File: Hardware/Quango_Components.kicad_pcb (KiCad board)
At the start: 4 copper layers, 80.8 x 100 mm, 186 parts, among them J1 Conn_01x12_Male, J2 Conn_01x16_Male, J3 Conn_01x12_Male, J4 Conn_01x12_Male, J5 SWD_Header, J6 Eurorack_10_pin_power, J7 Audio_Breakout, J8 Gate_Breakout, Q1 MMBT3904, U1 LM1117-3.3, U10 TL074, U11 TL074, U12 TL074, U13 TL074, U14 TL074, U15 TL074, U2 STM32G473V, U3 LM1117-5.0, U4 PS508, U5 MCP6002, U6 AS3364, U7 AS3364, U8 AD5676, U9 MCP48CMB21, Y1 8MHz 20pF

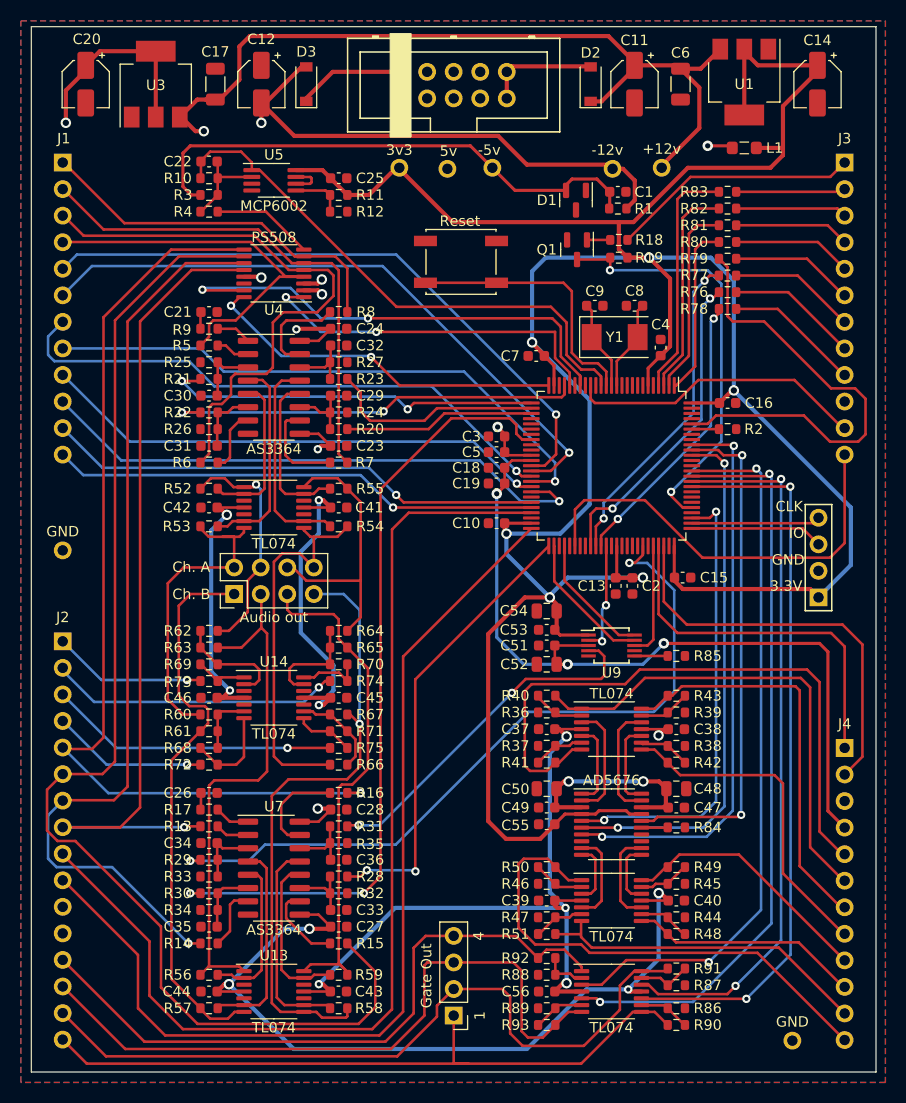
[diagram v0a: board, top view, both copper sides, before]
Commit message: Fixed OpAmp Power supply; component board annotations
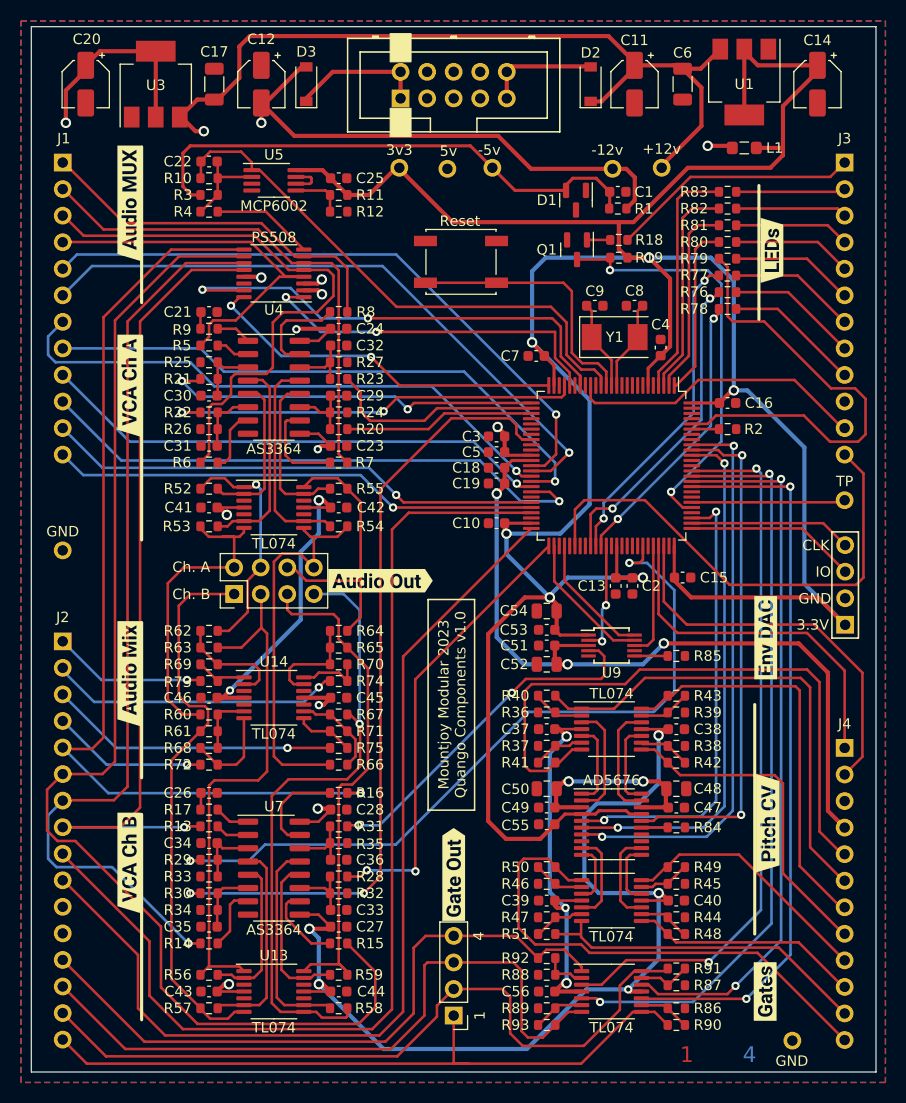
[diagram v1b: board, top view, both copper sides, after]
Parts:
- added FID1: Fiducial, Custom_Footprints:4_Layer_Markers, F.Cu at (115.8, 137.3)
- added J9: Test_Pin, Custom_Footprints:1mm_Test_Point, F.Cu at (127.9, 84.3)
- added kibuzzard-646A04C0: G***, kibuzzard-646A04C0, F.Cu at (59.5, 55.9)
- added kibuzzard-646A04E1: G***, kibuzzard-646A04E1, F.Cu at (59.5, 73.3)
- added kibuzzard-646A0551: G***, kibuzzard-646A0551, F.Cu at (59.5, 119.0)
- added kibuzzard-646A0570: G***, kibuzzard-646A0570, F.Cu at (59.5, 100.9)
- added kibuzzard-646A0602: G***, kibuzzard-646A0602, F.Cu at (83.5, 92.0)
- added kibuzzard-646A061F: G***, kibuzzard-646A061F, F.Cu at (90.5, 120.1)
- added kibuzzard-646A06F2: G***, kibuzzard-646A06F2, F.Cu at (120.5, 115.2)
- added kibuzzard-646A071F: G***, kibuzzard-646A071F, F.Cu at (120.3, 97.5)
- added kibuzzard-646A072B: G***, kibuzzard-646A072B, F.Cu at (120.3, 131.3)
- added kibuzzard-646A076E: G***, kibuzzard-646A076E, F.Cu at (121.0, 60.4)
- moved C41 12.4 mm to (67.1, 85.0), turned to 180 degrees
- moved C42 12.4 mm to (79.5, 85.0), turned to 0 degrees
- moved C44 12.4 mm to (79.5, 131.3), turned to 0 degrees
- moved C43 12.4 mm to (67.1, 131.3), turned to 180 degrees
- moved J5 3.66 mm to (128.0, 96.2)
- moved C6 0.20 mm to (112.4, 44.5)
- moved C17 0.10 mm to (67.6, 44.5)
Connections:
- U12 pad 11: +12V -> -12V
- U12 pad 4: -12V -> +12V
- U13 pad 11: +12V -> -12V
- U13 pad 4: -12V -> +12V
- U2 pad 81: unconnected-(U2-Pad81) -> Net-(U2-Pad81)
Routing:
- net Net-(U2-Pad81): track 0.00 -> 14.7 mm
- net /ChannelB_Level: track 41.0 -> 47.6 mm
- net +12V: track 258.8 -> 264.6 mm
- net -12V: track 257.8 -> 263.4 mm
- net +3.3V: track 310.6 -> 316.0 mm
- net /SWIO: track 12.8 -> 16.4 mm
- net /SWCLK: track 12.3 -> 15.5 mm
- net /USB_DP: track 39.2 -> 37.6 mm
- net /USB_DM: track 35.3 -> 34.0 mm
- net +3.3VA: track 227.7 -> 228.7 mm
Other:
- board text added: "Mountjoy Modular 2023 Quango Components v1.0"
- board text removed: "Audio out"
- board text removed: "Gate Out"

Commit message: Clean Up of Panel and Control boards
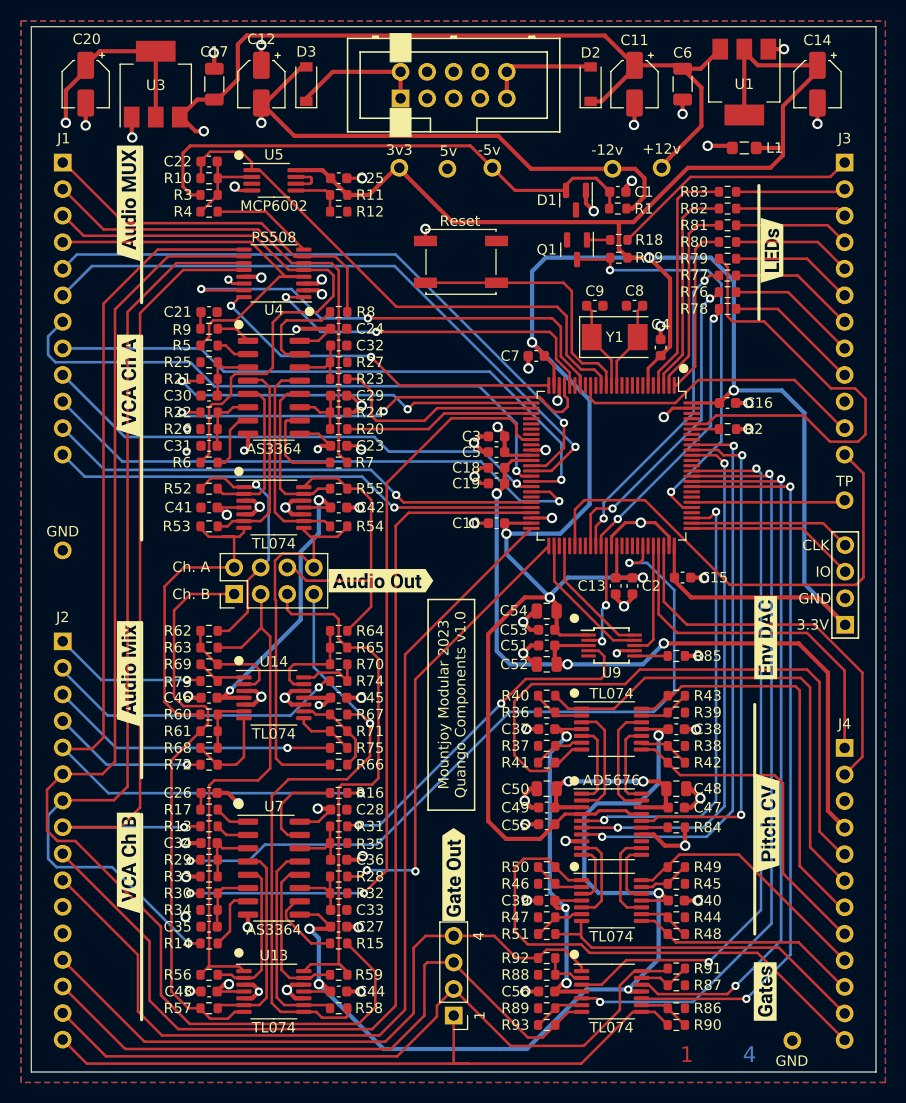
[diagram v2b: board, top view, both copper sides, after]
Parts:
- moved kibuzzard-646A04C0 0.05 mm to (59.4, 55.9)
- moved kibuzzard-646A04E1 0.05 mm to (59.4, 73.3)
- moved kibuzzard-646A0551 0.05 mm to (59.4, 119.0)
- moved kibuzzard-646A0570 0.05 mm to (59.4, 100.9)
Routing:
- net GND: track 0.00 -> 137.2 mm, vias 0 -> 65
- net /Gate3_Out: track 65.7 -> 62.4 mm
- net /OpAmps/AudioB3_Out: track 48.5 -> 51.5 mm
- net -12V: track 263.4 -> 266.3 mm
- net /Env1_Sustain: track 54.8 -> 57.4 mm
- net /EnvA2_DAC: track 39.9 -> 42.5 mm
- net /OpAmps/AudioA3_Out: track 27.2 -> 29.7 mm
- net /Env1_Release: track 55.7 -> 57.9 mm
- net /Gate2_Out: track 71.6 -> 69.5 mm
- net +3.3V: track 316.0 -> 317.9 mm
- net /OpAmps/AudioB1_Out: track 53.8 -> 55.2 mm
- net /Env1_Decay: track 61.4 -> 62.6 mm
- net /Audio3_Out: track 27.9 -> 29.0 mm
- net /AudioB3_In: track 118.9 -> 120.0 mm
- net /CV_OUT_A2: track 60.7 -> 61.6 mm
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
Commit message: Set up JLC parts placement details
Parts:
- moved TP3 0.10 mm to (89.9, 52.5)
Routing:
- net GND: vias 65 -> 67

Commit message: Updates to Panel Graphics
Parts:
- removed J9: Test_Pin, Custom_Footprints:1mm_Test_Point
- removed kibuzzard-646A04C0: G***, kibuzzard-646A04C0
- removed kibuzzard-646A04E1: G***, kibuzzard-646A04E1
- removed kibuzzard-646A0551: G***, kibuzzard-646A0551
- removed kibuzzard-646A0570: G***, kibuzzard-646A0570
- removed kibuzzard-646A071F: G***, kibuzzard-646A071F
- removed kibuzzard-646A072B: G***, kibuzzard-646A072B
- added kibuzzard-646B918A: G***, kibuzzard-646B918A, F.Cu at (59.4, 57.8)
- added kibuzzard-646B919C: G***, kibuzzard-646B919C, F.Cu at (59.5, 78.2)
- added kibuzzard-646B91AE: G***, kibuzzard-646B91AE, F.Cu at (59.4, 103.4)
- added kibuzzard-646B91BF: G***, kibuzzard-646B91BF, F.Cu at (59.4, 124.2)
- added kibuzzard-646B935C: G***, kibuzzard-646B935C, F.Cu at (120.3, 131.3)
- added kibuzzard-646B9368: G***, kibuzzard-646B9368, F.Cu at (120.3, 97.5)
- J3: value Conn_01x12_Male -> Conn_01x14_Male; footprint Connector_PinHeader_2.54mm:PinHeader_1x12_P2.54mm_Vertical -> Connector_PinHeader_2.54mm:PinHeader_1x14_P2.54mm_Vertical
- U5: footprint Package_SO:MSOP-8_3x3mm_P0.65mm -> Package_SO:SOIC-8_3.9x4.9mm_P1.27mm
- moved J5 0.68 mm to (128.0, 96.9)
- moved kibuzzard-646A06F2 0.38 mm to (120.6, 114.8)
- moved kibuzzard-646A076E 0.20 mm to (121.0, 60.6)
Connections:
- U2 pad 81: Net-(U2-Pad81) -> /Test_Pin2
- U2 pad 82: unconnected-(U2-Pad82) -> /Test_Pin1
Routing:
- net /Test_Pin1: track 0.00 -> 15.3 mm
- net /Test_Pin2: track 0.00 -> 14.8 mm
- net Net-(U2-Pad81): track 14.7 -> 0.00 mm
- net /Gate4: track 69.0 -> 74.3 mm
- net GND: track 137.2 -> 138.4 mm, vias 67 -> 135
- net +3.3V: track 317.9 -> 319.0 mm
- net /ChannelB_Level: track 47.6 -> 48.4 mm
- net /Audio_In_Multiplexed: track 52.7 -> 53.5 mm
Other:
- board text added: "MCP48C"

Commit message: Final Updates for v1.0 production
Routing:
- net GND: track 138.4 -> 138.7 mm, vias 135 -> 134
